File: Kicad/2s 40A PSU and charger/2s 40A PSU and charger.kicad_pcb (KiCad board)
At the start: 4 copper layers, 45 x 20 mm, 111 parts, among them J1 Keystone 3579, J10 USB_C_Receptacle_USB2.0_16P, J11 1.27mm 4 pin socket, J12 USB, J2 JST XH-S Balance Plug, J3 Keystone 3579, J4 Keystone 3569, J5 Keystone 3569, J6 Keystone 3579, J7 Keystone 3579, J8 Keystone 3569, J9 Keystone 3569, Q1 PJA3430, Q2 PJA3430, Q3 Vishay sir404dp, or SiR500DP, Q4 PJA3430, Q5 PJA3430, Q6 Vishay sir404dp, or SiR500DP, U1 BQ76905RGRR, U2 AP63203WU, U3 BQ24780SRUYR, U5 THVD1420DRLR, U6 CH32X035G8U6, U7 TPS7A2633DRV

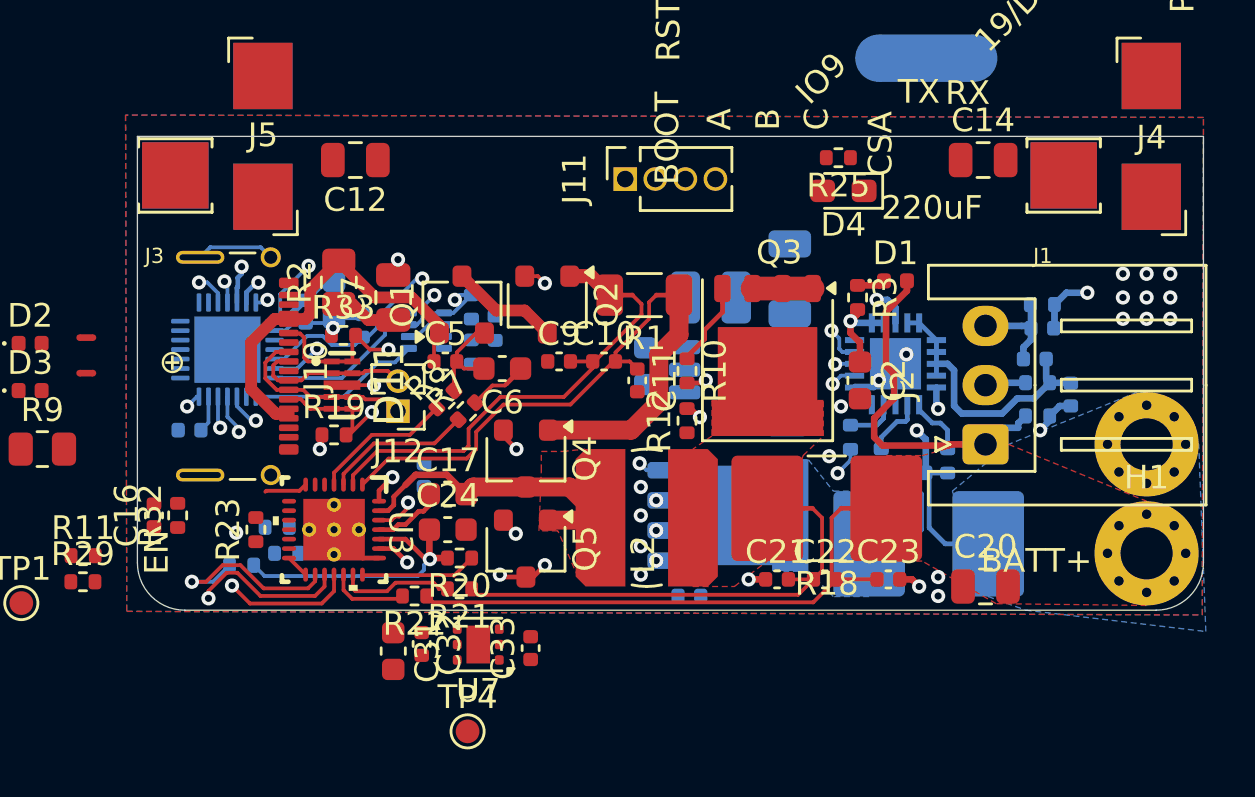
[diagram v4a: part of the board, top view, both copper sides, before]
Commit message: Reorient 3v3 main PSU
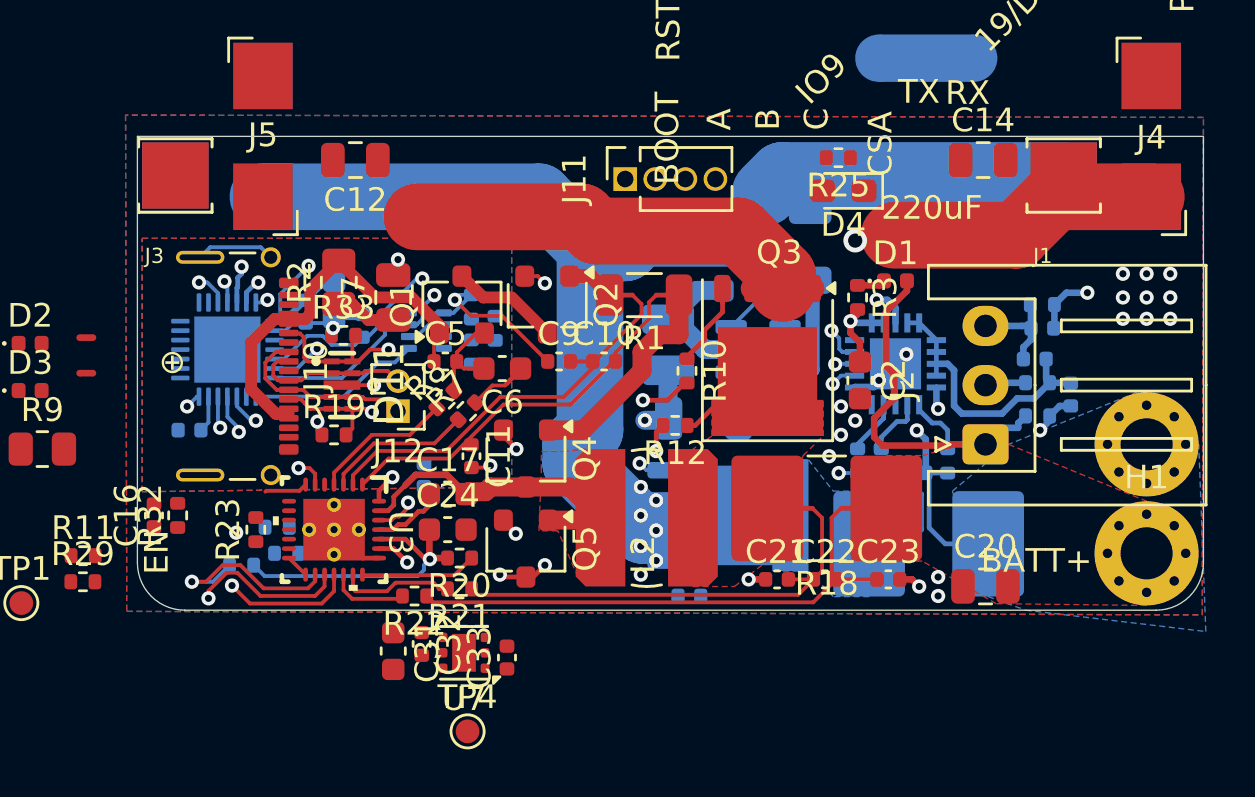
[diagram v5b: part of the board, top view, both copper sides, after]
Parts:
- moved C11 7.70 mm to (122.2, 125.5)
- moved C27 6.92 mm to (132.0, 123.9), turned to 0 degrees
- moved C28 6.09 mm to (136.5, 116.6), turned to 90 degrees
- moved C40 5.17 mm to (133.6, 118.5), turned to 180 degrees
- moved L3 2.69 mm to (130.5, 120.8), turned to -90 degrees
- moved U2 2.14 mm to (134.3, 121.0)
- moved C33 1.08 mm to (123.7, 134.0)
- moved R6 1.04 mm to (138.5, 125.7)
- moved U7 0.69 mm to (121.9, 133.8)
- moved R12 0.54 mm to (130.8, 124.2), turned to 180 degrees
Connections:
- U7 pad 7: (no net) -> GNDPWR
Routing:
- net GNDPWR: track 9.63 -> 57.5 mm, vias 25 -> 27
- net /Battery Charger/MOTORPWR: track 2.54 -> 38.0 mm, vias 0 -> 1
- net Net-(U2-SW): track 0.00 -> 6.02 mm
- net GND: track 10.4 -> 16.3 mm, vias 6 -> 7
- net Net-(Q3-S): track 0.00 -> 4.65 mm
- net /Battery Charger/IN: track 20.3 -> 16.7 mm
- net /Connectors/3.3v: track 0.00 -> 3.08 mm, vias 0 -> 1
- net /Battery Balancer/Low: track 15.0 -> 18.0 mm
- net Net-(U2-BST): track 0.00 -> 2.05 mm
- net Net-(U3-ACN): track 17.8 -> 16.3 mm
- net /Battery Charger/PWRON: track 0.00 -> 1.26 mm, vias 0 -> 1
- net Net-(U3-BATDRV): track 30.6 -> 29.6 mm
- net Net-(U3-BATSRC): track 31.9 -> 31.1 mm
- net Net-(Q4-D): track 8.36 -> 7.65 mm
- added copper zone on B.Cu, net GND
- added copper zone on F.Cu, net GND
- added copper zone on In1.Cu, net GND
- added copper zone on In2.Cu, net GND

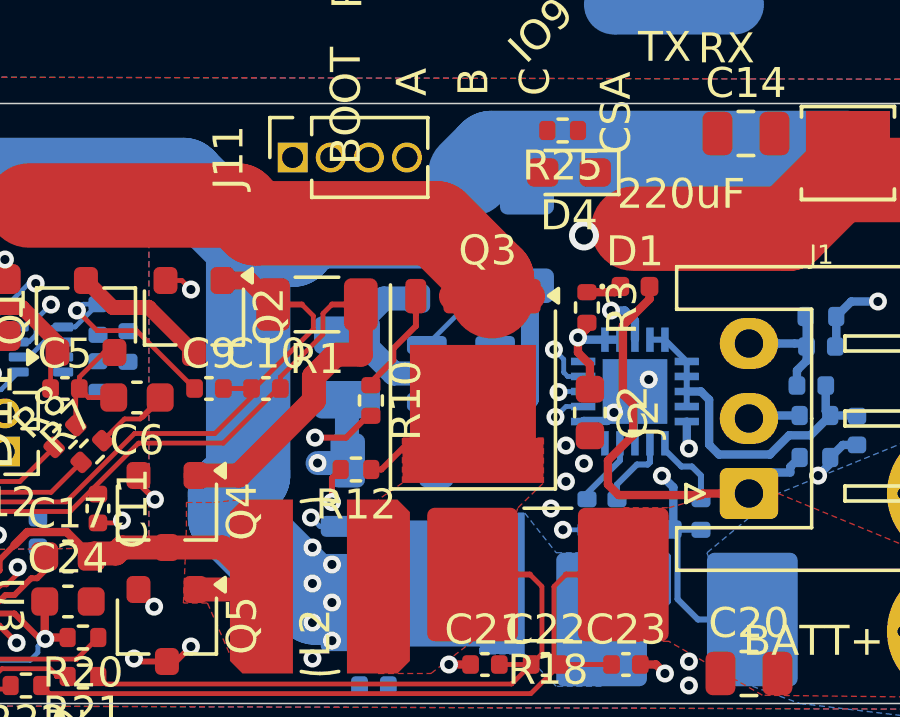
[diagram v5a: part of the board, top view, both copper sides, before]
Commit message: Changed default via sizes
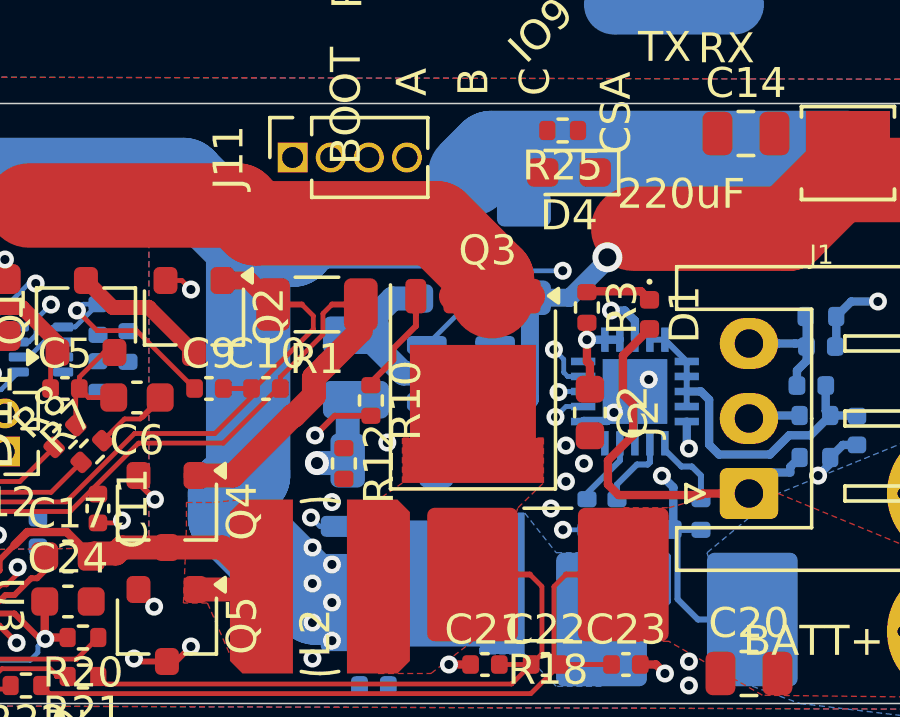
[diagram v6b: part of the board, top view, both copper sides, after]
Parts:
- moved D1 1.05 mm to (140.6, 119.0), turned to -90 degrees
- moved NT4 0.80 mm to (130.4, 120.1), turned to 45 degrees
- moved R12 0.45 mm to (130.4, 124.0), turned to -90 degrees
- moved C28 0.41 mm to (136.4, 117.0)
- moved L3 0.30 mm to (130.8, 120.8)
- moved C40 0.10 mm to (133.7, 118.5)
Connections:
- U1 pad 11: GNDPWR -> /Battery Balancer/-BAT
- U1 pad 21: GNDPWR -> /Battery Balancer/-BAT
- U1 pad 8: GNDPWR -> /Battery Balancer/-BAT
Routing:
- net GNDPWR: track 57.5 -> 52.4 mm, vias 27 -> 26
- net /Battery Balancer/-BAT: track 24.4 -> 29.5 mm, vias 1 -> 3
- net /Connectors/3.3v: track 3.08 -> 8.03 mm, vias 1 -> 2
- net Net-(Q3-S): track 4.65 -> 0.00 mm
- net /Battery Charger/MOTORPWR: track 38.0 -> 40.5 mm
- net Net-(D1-A): track 10.8 -> 9.37 mm
- net Net-(Q4-D): track 7.65 -> 6.26 mm
- net Net-(U3-BATSRC): track 31.1 -> 29.9 mm
- net Net-(D1-K): track 1.19 -> 2.22 mm
- net Net-(U1-BAT): track 3.93 -> 3.36 mm
- net Net-(U2-SW): track 6.02 -> 5.52 mm

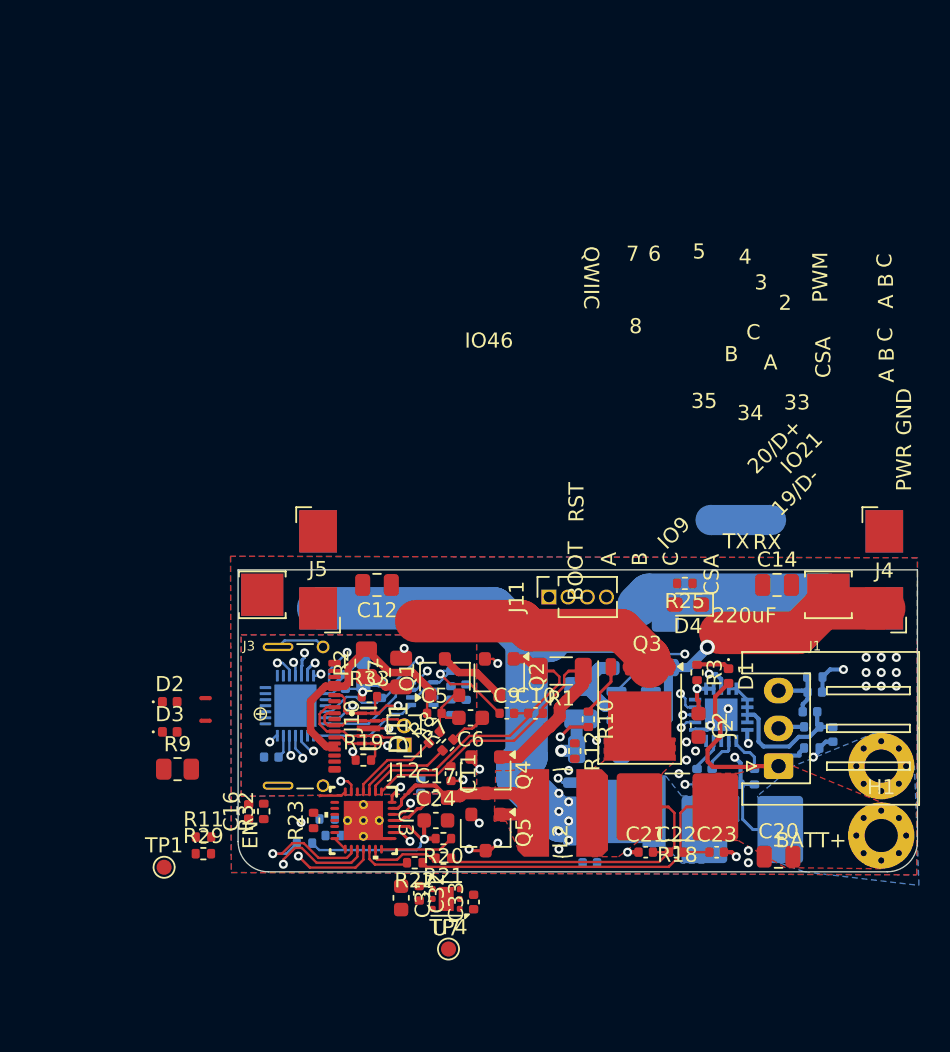
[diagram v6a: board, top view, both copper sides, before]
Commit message: Removed snubber from USB shield and connected direct to GND
This saves on components, and as far as good/bad RF practicalities go, many people are split on the practicality of it. I will go with the simpler method
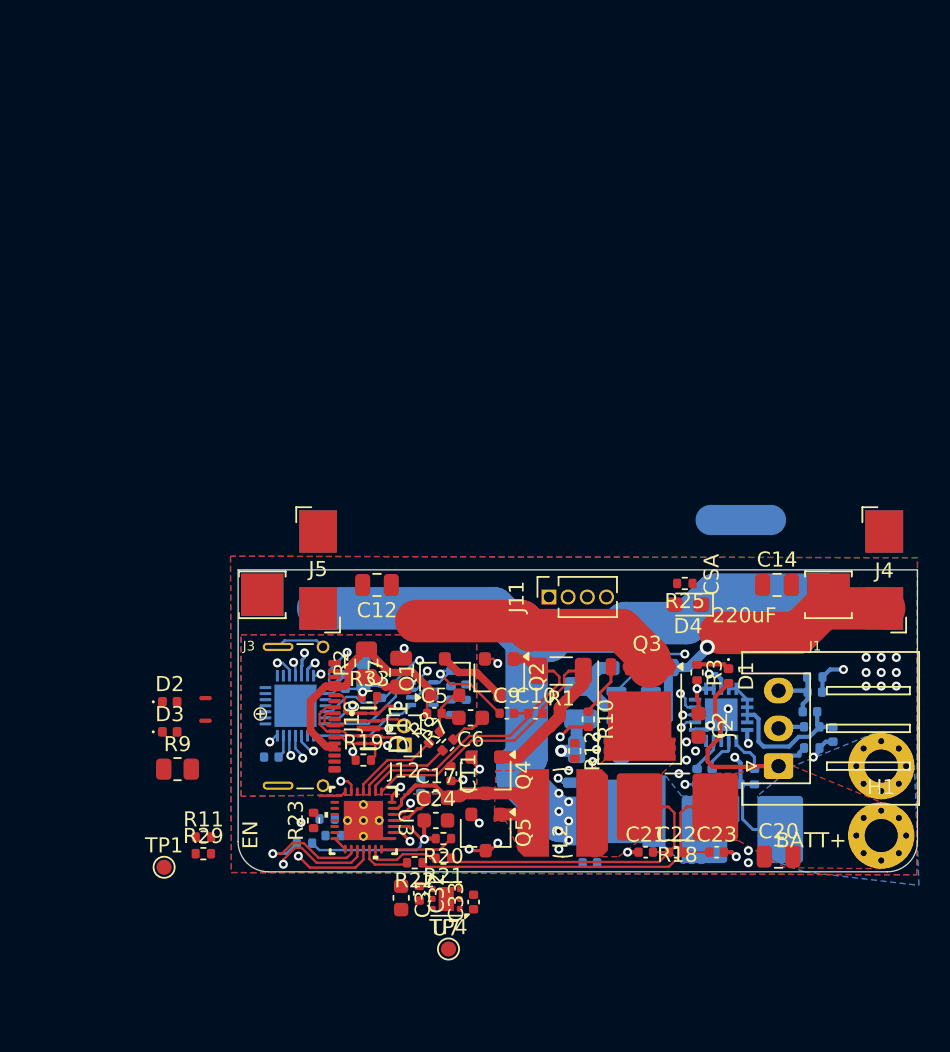
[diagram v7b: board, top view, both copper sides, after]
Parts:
- removed C16: 100nF, Capacitor_SMD:C_0402_1005Metric
- removed R32: 100k, Resistor_SMD:R_0402_1005Metric
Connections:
- J10 pad A1: GNDPWR -> GND
- J10 pad A12: GNDPWR -> GND
- J10 pad B1: GNDPWR -> GND
- J10 pad B12: GNDPWR -> GND
- J10 pad GND: GNDPWR -> GND
- J10 pad S1: Net-(J10-SHIELD) -> GND
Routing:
- net GND: track 16.3 -> 19.6 mm
- net Net-(J10-SHIELD): track 3.33 -> 0.00 mm
- net GNDPWR: track 52.4 -> 54.6 mm, vias 26 -> 28
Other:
- board text added: "2s 40A PSU"
- board text removed: "19/D-"
- board text removed: "2"
- board text removed: "20/D+"
- board text removed: "3"
- board text removed: "3.3v"
- board text removed: "33"
- board text removed: "34"
- board text removed: "35"
- board text removed: "4"
- board text removed: "5"
- board text removed: "6"
- board text removed: "7"
- board text removed: "8"
- board text removed: "A"
- board text removed: "B"
- board text removed: "BOOT"
- board text removed: "C"
- board text removed: "CS0"
- board text removed: "ESP32-s3 motor pcb V2"
- board text removed: "Encoder"
- board text removed: "GND"
- board text removed: "IO21"
- board text removed: "IO46"
- board text removed: "IO9"
- board text removed: "PWM"
- board text removed: "PWR"
- board text removed: "QWIIC"
- board text removed: "RST"
- board text removed: "RX"
- board text removed: "SCL"
- board text removed: "SDA"
- board text removed: "TX"
- board text removed: "|||||||"

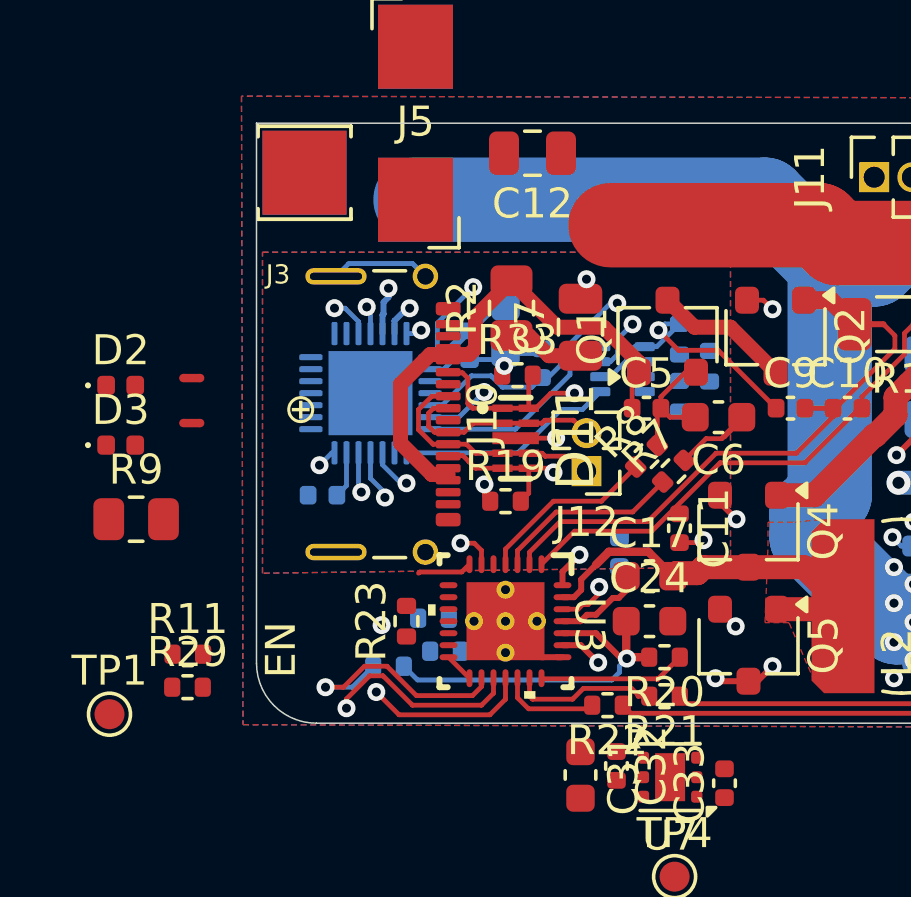
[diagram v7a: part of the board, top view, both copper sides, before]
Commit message: Disconnect REGN from unneeded output pullups
These pullups will instead be pulled to 3v3, which should be closer locally. I don't use them but pullups are required for internal detection.
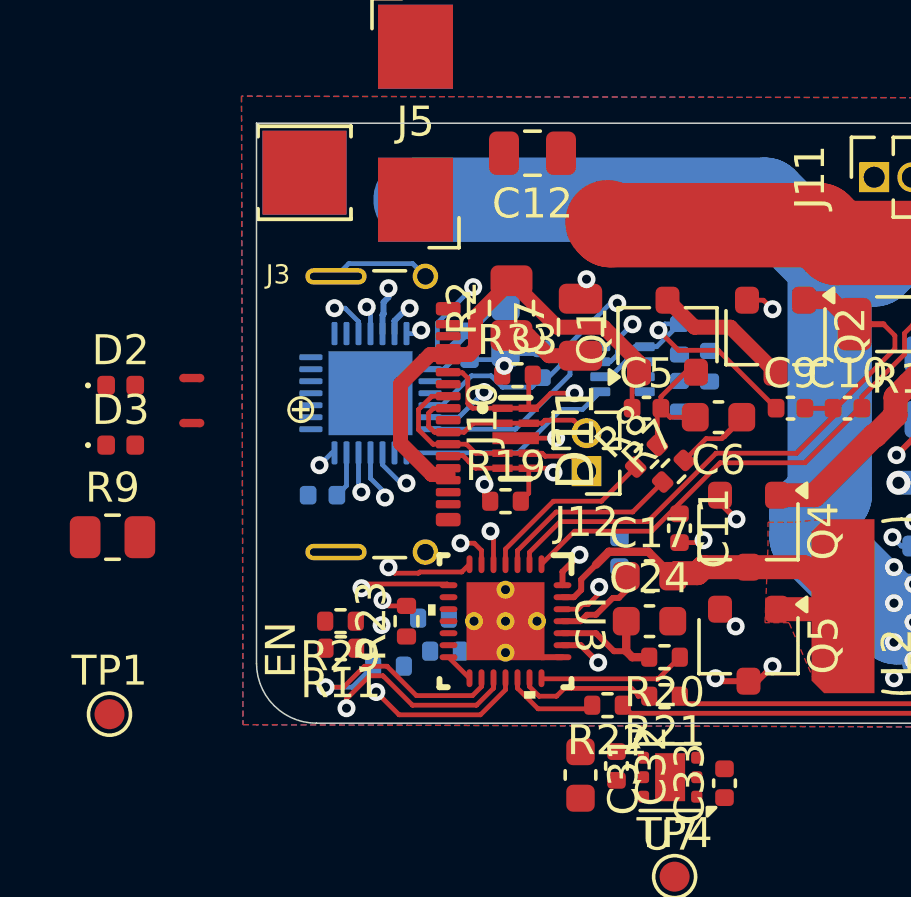
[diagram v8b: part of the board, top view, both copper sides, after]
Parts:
- moved R29 5.55 mm to (110.9, 128.6), turned to 180 degrees
- moved R11 5.10 mm to (110.9, 129.5), turned to 180 degrees
- moved R9 0.99 mm to (103.3, 125.8)
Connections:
- C25 pad 1: /MCU/3.3v -> /Battery Charger/MCU3.3v
- C26 pad 1: /MCU/3.3v -> /Battery Charger/MCU3.3v
- C33 pad 1: /MCU/3.3v -> /Battery Charger/MCU3.3v
- R11 pad 2: /MCU/3.3v -> /Battery Charger/MCU3.3v
- R23 pad 1: /Battery Charger/REGN -> /Battery Charger/MCU3.3v
- R24 pad 1: /Battery Charger/REGN -> /Battery Charger/MCU3.3v
- R28 pad 1: /MCU/3.3v -> /Battery Charger/MCU3.3v
- R29 pad 2: /MCU/3.3v -> /Battery Charger/MCU3.3v
- U5 pad 8: /MCU/3.3v -> /Battery Charger/MCU3.3v
- U6 pad 2: /MCU/3.3v -> /Battery Charger/MCU3.3v
- U7 pad 1: /MCU/3.3v -> /Battery Charger/MCU3.3v
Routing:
- net /Battery Charger/REGN: track 12.6 -> 4.22 mm, vias 1 -> 0
- net /MCU/3.3v: track 3.64 -> 0.00 mm
- net /Battery Charger/MCU3.3v: track 0.00 -> 3.64 mm
- net /Battery Charger/Charger IDCHG: track 1.55 -> 4.52 mm, vias 0 -> 1
- net Net-(U3-ACOK): track 0.00 -> 2.02 mm, vias 0 -> 2
- net /Battery Charger/Charger IADP: track 10.0 -> 11.1 mm, vias 1 -> 2
- removed copper zone on B.Cu, net GND
- removed copper zone on F.Cu, net GND
- removed copper zone on In1.Cu, net GND
- removed copper zone on In2.Cu, net GND
